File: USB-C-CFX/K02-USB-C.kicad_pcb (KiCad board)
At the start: 2 copper layers, 98.3 x 87.7 mm, 31 parts, among them SW1 SW_Push, SW10 SW_Push, SW11 SW_Push, SW12 SW_Push, SW13 SW_Push, SW14 SW_Push, SW15 SW_Push, SW16 SW_Push, SW17 SW_Push, SW18 SW_Push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

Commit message: upsie
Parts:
- moved ? 1.25 mm to (60.5, 103.2)
- moved ? 0.88 mm to (58.7, 91.0)
- moved ? 0.88 mm to (60.8, 91.0)
- moved B+ 0.88 mm to (23.9, 105.7)
- moved U1 0.88 mm to (40.9, 98.0)
- moved B- 0.88 mm to (23.9, 90.8)
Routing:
- net Switch10: track 101.9 -> 103.3 mm
- net Switch18: track 143.0 -> 144.4 mm
- net reset: track 76.4 -> 77.2 mm
- net Switch9: track 63.1 -> 64.0 mm
- net Switch8: track 49.4 -> 50.3 mm
- net Switch7: track 48.2 -> 49.1 mm
- net vcc: track 72.5 -> 73.3 mm
- net Switch12: track 25.1 -> 26.0 mm
- net raw: track 69.5 -> 70.3 mm
- net Switch13: track 39.8 -> 40.6 mm
- net Switch16: track 51.3 -> 52.0 mm
- net Switch1: track 54.6 -> 55.3 mm
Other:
- board size 98.3 x 87.7 mm -> 98.4 x 88.6 mm

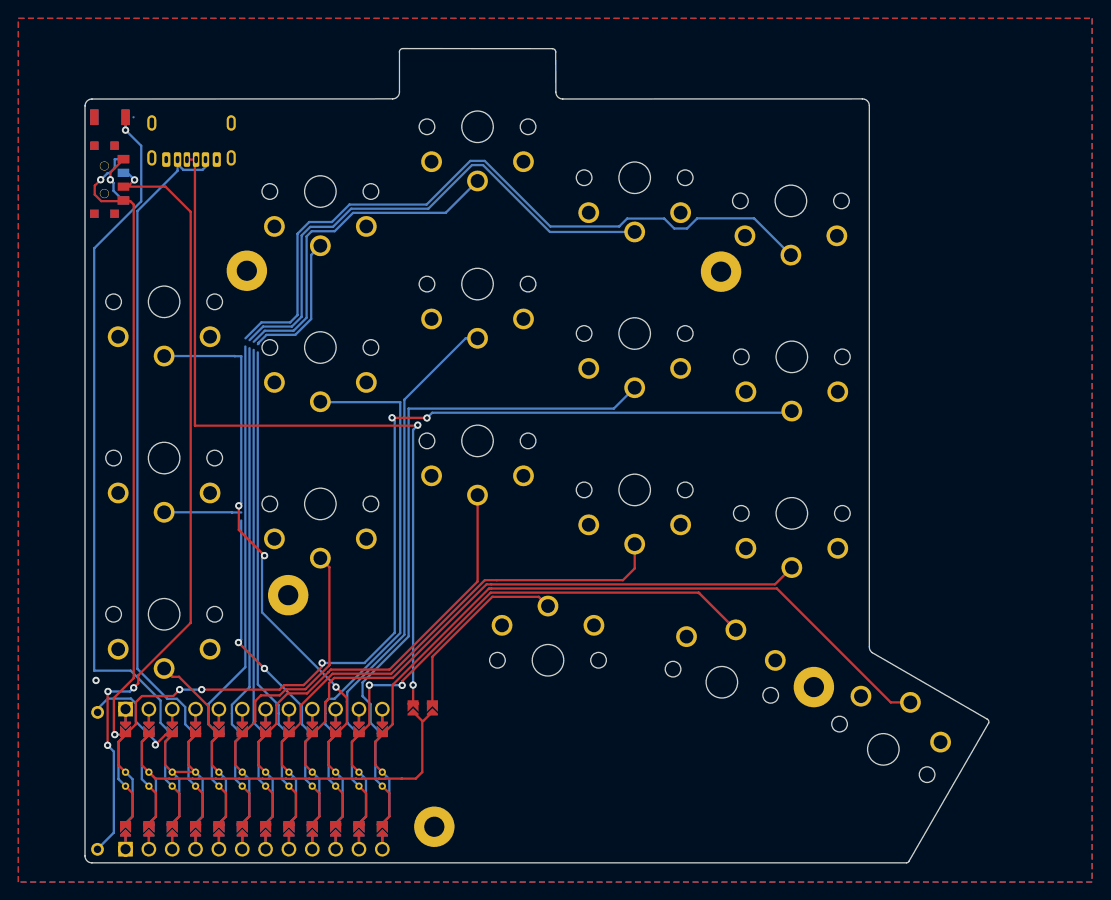
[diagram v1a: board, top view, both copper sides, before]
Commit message: what
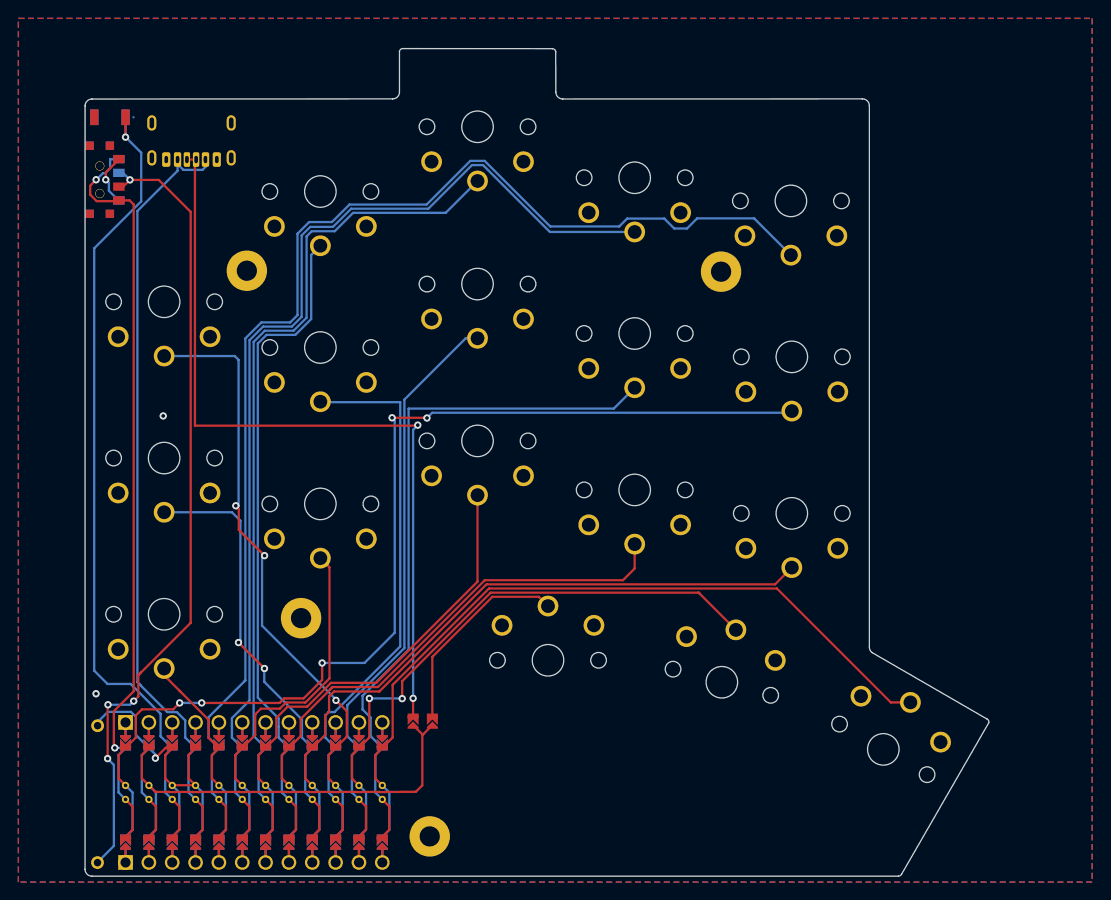
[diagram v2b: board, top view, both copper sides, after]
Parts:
- removed the ? at (60.5, 103.2)
- moved ? 44.8 mm to (60.0, 104.2)
- moved ? 2.87 mm to (46.0, 80.5)
- moved ? 1.45 mm to (58.7, 92.4)
- moved ? 1.45 mm to (60.8, 92.4)
- moved B+ 1.45 mm to (23.9, 107.1)
- moved B- 1.45 mm to (23.9, 92.2)
- moved U1 1.45 mm to (40.9, 99.5)
- moved POWER SW 0.50 mm to (24.1, 32.8)
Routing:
- net Switch18: track 144.4 -> 147.3 mm
- net Switch5: track 124.9 -> 127.3 mm
- net Switch2: track 58.4 -> 60.7 mm
- net Switch4: track 101.3 -> 103.6 mm
- net Switch3: track 79.2 -> 81.5 mm
- net raw: track 70.3 -> 72.4 mm
- net vcc: track 73.3 -> 75.3 mm
- net BT+_r: track 86.0 -> 87.9 mm
- net Switch6: track 35.2 -> 36.8 mm
- net Switch16: track 52.0 -> 53.5 mm
- net Switch7: track 49.1 -> 50.6 mm
- net Switch8: track 50.3 -> 51.7 mm
- net Switch17: track 71.7 -> 73.1 mm
- net Switch10: track 103.3 -> 104.7 mm
- net Switch9: track 64.0 -> 65.4 mm
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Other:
- board size 98.4 x 88.6 mm -> 98.4 x 90.1 mm

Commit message: here we go again
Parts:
- moved ? 1.25 mm to (60.0, 103.0)
- moved ? 0.83 mm to (91.2, 43.5)
- moved ? 0.10 mm to (40.0, 42.7)
